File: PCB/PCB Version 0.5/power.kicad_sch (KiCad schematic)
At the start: 31 parts, among them IC5 LMR38025SDRRR, IC6 LMR38025SDRRR, U4 TPS2116DRL, U6 LP5912-3.3DRV, U7 TPS746-3.3DRV

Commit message: wip backup
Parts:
- C72: footprint Capacitor_SMD:C_1210_3225Metric -> Capacitor_SMD:C_0805_2012Metric
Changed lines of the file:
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@@
 			)
 		)
-		(property "Footprint" "Capacitor_SMD:C_1210_3225Metric"
+		(property "Footprint" "Capacitor_SMD:C_0805_2012Metric"
 			(at 147.0152 127 0)
 			(effects

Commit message: wip backup
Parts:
- C67, C70: footprint Capacitor_SMD:C_0402_1005Metric -> Capacitor_SMD:C_0402_1005Metric_Pad0.74x0.62mm_HandSolder
- R15, R16, R19, R20: footprint Resistor_SMD:R_0402_1005Metric -> Resistor_SMD:R_0402_1005Metric_Pad0.72x0.64mm_HandSolder
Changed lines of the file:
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@@
 			)
 		)
-		(property "Footprint" "Resistor_SMD:R_0402_1005Metric"
+		(property "Footprint" "Resistor_SMD:R_0402_1005Metric_Pad0.72x0.64mm_HandSolder"
 			(at 125.222 118.11 90)
 			(effects
@@
 			)
 		)
-		(property "Footprint" "Resistor_SMD:R_0402_1005Metric"
+		(property "Footprint" "Resistor_SMD:R_0402_1005Metric_Pad0.72x0.64mm_HandSolder"
 			(at 125.222 128.27 90)
 			(effects
@@
 			)
 		)
-		(property "Footprint" "Capacitor_SMD:C_0402_1005Metric"
+		(property "Footprint" "Capacitor_SMD:C_0402_1005Metric_Pad0.74x0.62mm_HandSolder"
 			(at 53.0352 68.58 0)
 			(effects
@@
 			)
 		)
-		(property "Footprint" "Capacitor_SMD:C_0402_1005Metric"
+		(property "Footprint" "Capacitor_SMD:C_0402_1005Metric_Pad0.74x0.62mm_HandSolder"
 			(at 53.0352 130.81 0)
 			(effects
@@
 			)
 		)
-		(property "Footprint" "Resistor_SMD:R_0402_1005Metric"
+		(property "Footprint" "Resistor_SMD:R_0402_1005Metric_Pad0.72x0.64mm_HandSolder"
 			(at 125.222 66.04 90)
 			(effects
@@
 			)
 		)
-		(property "Footprint" "Resistor_SMD:R_0402_1005Metric"
+		(property "Footprint" "Resistor_SMD:R_0402_1005Metric_Pad0.72x0.64mm_HandSolder"
 			(at 125.222 55.88 90)
 			(effects

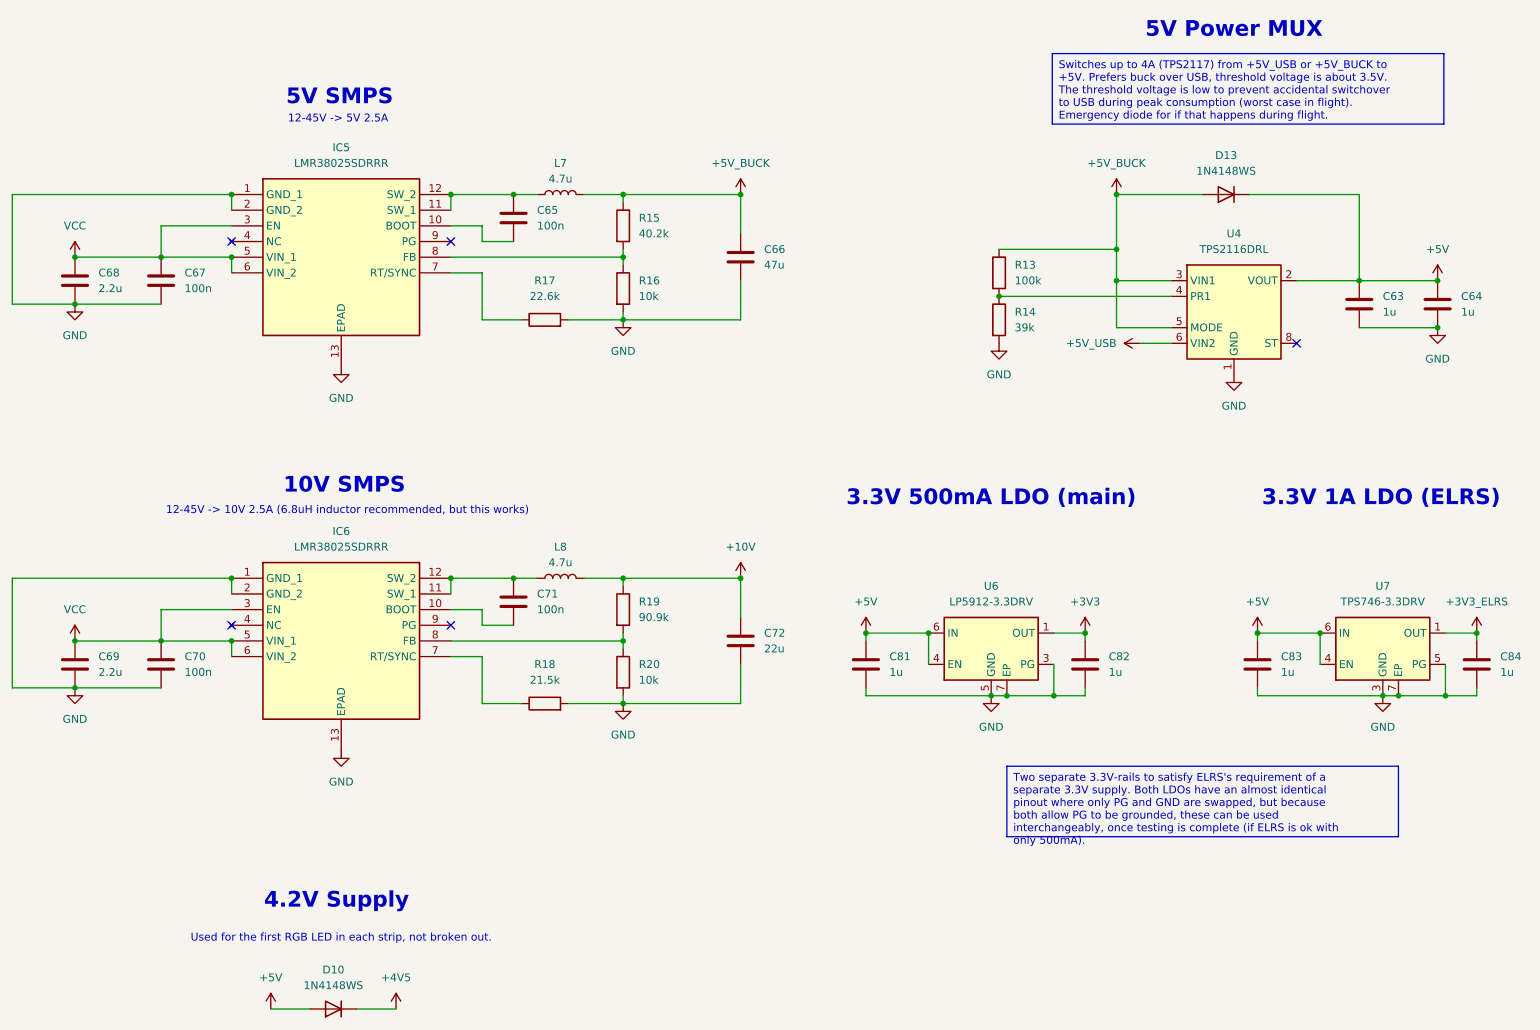
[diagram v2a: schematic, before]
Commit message: preliminary layout
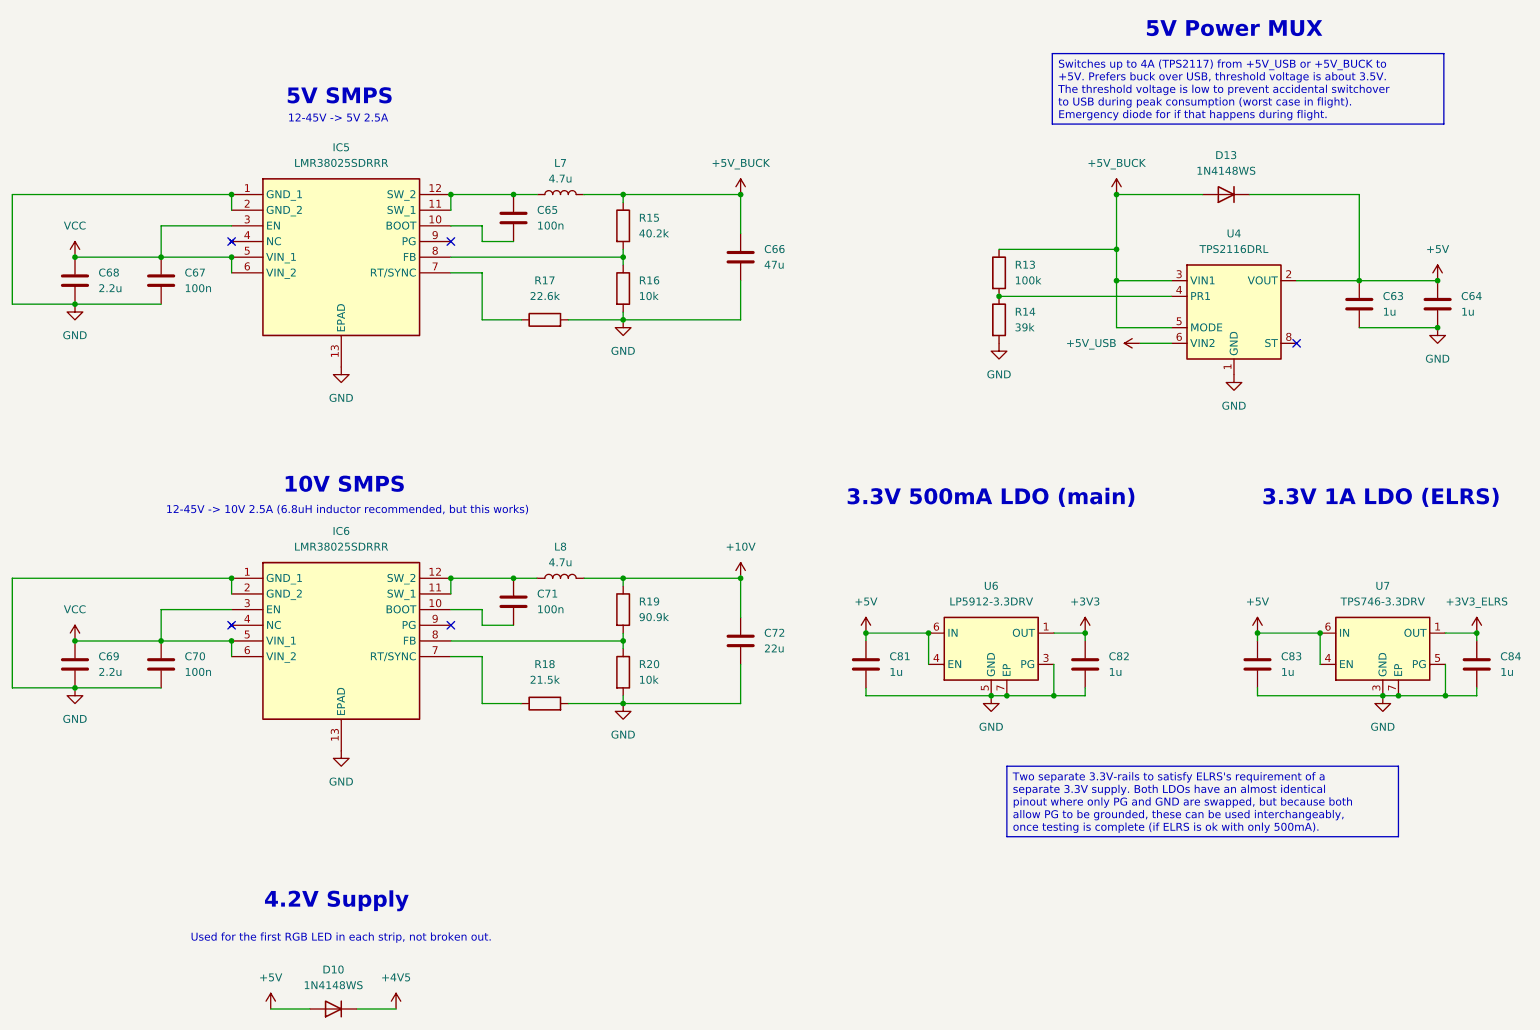
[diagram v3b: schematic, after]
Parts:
- C65, C71, C84: footprint Capacitor_SMD:C_0402_1005Metric -> Capacitor_SMD:C_0402_1005Metric_Pad0.74x0.62mm_HandSolder
- C67: footprint Capacitor_SMD:C_0402_1005Metric_Pad0.74x0.62mm_HandSolder -> Capacitor_SMD:C_0402_1005Metric
- R13, R14, R17, R18: footprint Resistor_SMD:R_0402_1005Metric -> Resistor_SMD:R_0402_1005Metric_Pad0.72x0.64mm_HandSolder
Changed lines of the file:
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@@
 (kicad_sch
-	(version 20231120)
+	(version 20250114)
 	(generator "eeschema")
-	(generator_version "8.0")
+	(generator_version "9.0")
 	(paper "A4")
 	(title_block
 		(title "Kolibri FC - DCDC + LDO")
 	)
+	(text "12-45V -> 10V 2.5A (6.8uH inductor recommended, but this works)"
+		(exclude_from_sim no)
+		(at 82.296 102.108 0)
+		(effects
+			(font
+				(size 1.27 1.27)
+			)
+		)
+	)
+	(text "3.3V 1A LDO (ELRS)"
+		(exclude_from_sim no)
+		(at 249.936 100.076 0)
+		(effects
+			(font
+				(size 2.54 2.54)
+				(thickness 0.508)
+				(bold yes)
+			)
+		)
+	)
+	(text "Used for the first RGB LED in each strip, not broken out."
+		(exclude_from_sim no)
+		(at 81.28 171.45 0)
+		(effects
+			(font
+				(size 1.27 1.27)
+			)
+		)
+	)
+	(text "12-45V -> 5V 2.5A"
+		(exclude_from_sim no)
+		(at 80.772 38.608 0)
+		(effects
+			(font
+				(size 1.27 1.27)
+			)
+		)
+	)
+	(text "3.3V 500mA LDO (main)"
+		(exclude_from_sim no)
+		(at 186.69 100.076 0)
+		(effects
+			(font
+				(size 2.54 2.54)
+				(thickness 0.508)
+				(bold yes)
+			)
+		)
+	)
+	(text "4.2V Supply"
+		(exclude_from_sim no)
+		(at 80.518 165.354 0)
+		(effects
+			(font
+				(size 2.54 2.54)
+				(thickness 0.508)
+				(bold yes)
+			)
+		)
+	)
+	(text "5V SMPS"
+		(exclude_from_sim no)
+		(at 81.026 35.052 0)
+		(effects
+			(font
+				(size 2.54 2.54)
+				(thickness 0.508)
+				(bold yes)
+			)
+		)
+	)
+	(text "5V Power MUX"
+		(exclude_from_sim no)
+		(at 226.06 24.13 0)
+		(effects
+			(font
+				(size 2.54 2.54)
+				(thickness 0.508)
+				(bold yes)
+			)
+		)
+	)
+	(text "10V SMPS"
+		(exclude_from_sim no)
+		(at 81.788 98.044 0)
+		(effects
+			(font
+				(size 2.54 2.54)
+				(thickness 0.508)
+				(bold yes)
+			)
+		)
+	)
+	(text_box "Two separate 3.3V-rails to satisfy ELRS's requirement of a separate 3.3V supply. Both LDOs have an almost identical pinout where only PG and GND are swapped, but because both allow PG to be grounded, these can be used interchangeably, once testing is complete (if ELRS is ok with only 500mA)."
+		(exclude_from_sim no)
+		(at 189.23 143.51 0)
+		(size 63.5 11.43)
+		(margins 0.9525 0.9525 0.9525 0.9525)
+		(stroke
+			(width 0)
+			(type default)
+		)
+		(fill
+			(type none)
+		)
+		(effects
+			(font
+				(size 1.27 1.27)
+			)
+			(justify left top)
+		)
+	)
+	(text_box "Switches up to 4A (TPS2117) from +5V_USB or +5V_BUCK to +5V. Prefers buck over USB, threshold voltage is about 3.5V. The threshold voltage is low to prevent accidental switchover to USB during peak consumption (worst case in flight). Emergency diode for if that happens during flight."
+		(exclude_from_sim no)
+		(at 196.596 27.94 0)
+		(size 63.5 11.43)
+		(margins 0.9525 0.9525 0.9525 0.9525)
+		(stroke
+			(width 0)
+			(type default)
+		)
+		(fill
+			(type none)
+		)
+		(effects
+			(font
+				(size 1.27 1.27)
+			)
+			(justify left top)
+		)
+	)
 	(junction
 		(at 146.05 113.03)
@@
 		)
 	)
-	(text_box "Two separate 3.3V-rails to satisfy ELRS's requirement of a separate 3.3V supply. Both LDOs have an almost identical pinout where only PG and GND are swapped, but because both allow PG to be grounded, these can be used interchangeably, once testing is complete (if ELRS is ok with only 500mA)."
-		(exclude_from_sim no)
-		(at 189.23 143.51 0)
-		(size 63.5 11.43)
-		(stroke
-			(width 0)
-			(type default)
-		)
-		(fill
-			(type none)
-		)
-		(effects
-			(font
-				(size 1.27 1.27)
-			)
-			(justify left top)
-		)
-	)
-	(text_box "Switches up to 4A (TPS2117) from +5V_USB or +5V_BUCK to +5V. Prefers buck over USB, threshold voltage is about 3.5V. The threshold voltage is low to prevent accidental switchover to USB during peak consumption (worst case in flight). Emergency diode for if that happens during flight."
-		(exclude_from_sim no)
-		(at 196.596 27.94 0)
-		(size 63.5 11.43)
-		(stroke
-			(width 0)
-			(type default)
-		)
-		(fill
-			(type none)
-		)
-		(effects
-			(font
-				(size 1.27 1.27)
-			)
-			(justify left top)
-		)
-	)
-	(text "12-45V -> 10V 2.5A (6.8uH inductor recommended, but this works)"
-		(exclude_from_sim no)
-		(at 82.296 102.108 0)
-		(effects
-			(font
-				(size 1.27 1.27)
-			)
-		)
-	)
-	(text "3.3V 1A LDO (ELRS)"
-		(exclude_from_sim no)
-		(at 249.936 100.076 0)
-		(effects
-			(font
-				(size 2.54 2.54)
-				(thickness 0.508)
-				(bold yes)
-			)
-		)
-	)
-	(text "Used for the first RGB LED in each strip, not broken out."
-		(exclude_from_sim no)
-		(at 81.28 171.45 0)
-		(effects
-			(font
-				(size 1.27 1.27)
-			)
-		)
-	)
-	(text "12-45V -> 5V 2.5A"
-		(exclude_from_sim no)
-		(at 80.772 38.608 0)
-		(effects
-			(font
-				(size 1.27 1.27)
-			)
-		)
-	)
-	(text "3.3V 500mA LDO (main)"
-		(exclude_from_sim no)
-		(at 186.69 100.076 0)
-		(effects
-			(font
-				(size 2.54 2.54)
-				(thickness 0.508)
-				(bold yes)
-			)
-		)
-	)
-	(text "4.2V Supply"
-		(exclude_from_sim no)
-		(at 80.518 165.354 0)
-		(effects
-			(font
-				(size 2.54 2.54)
-				(thickness 0.508)
-				(bold yes)
-			)
-		)
-	)
-	(text "5V SMPS"
-		(exclude_from_sim no)
-		(at 81.026 35.052 0)
-		(effects
-			(font
-				(size 2.54 2.54)
-				(thickness 0.508)
-				(bold yes)
-			)
-		)
-	)
-	(text "5V Power MUX"
-		(exclude_from_sim no)
-		(at 226.06 24.13 0)
-		(effects
-			(font
-				(size 2.54 2.54)
-				(thickness 0.508)
-				(bold yes)
-			)
-		)
-	)
-	(text "10V SMPS"
-		(exclude_from_sim no)
-		(at 81.788 98.044 0)
-		(effects
-			(font
-				(size 2.54 2.54)
-				(thickness 0.508)
-				(bold yes)
-			)
-		)
-	)
 	(symbol
 		(lib_id "Device:C")
@@
 			)
 		)
-		(property "Footprint" "Resistor_SMD:R_0402_1005Metric"
+		(property "Footprint" "Resistor_SMD:R_0402_1005Metric_Pad0.72x0.64mm_HandSolder"
 			(at 186.182 63.5 90)
 			(effects
@@
 			)
 		)
-		(property "Footprint" "Resistor_SMD:R_0402_1005Metric"
+		(property "Footprint" "Resistor_SMD:R_0402_1005Metric_Pad0.72x0.64mm_HandSolder"
 			(at 114.3 72.898 90)
 			(effects
@@
 			)
 		)
-		(property "Footprint" "Resistor_SMD:R_0402_1005Metric"
+		(property "Footprint" "Resistor_SMD:R_0402_1005Metric_Pad0.72x0.64mm_HandSolder"
 			(at 114.3 135.128 90)
 			(effects
@@
 			)
 		)
-		(property "Footprint" "Capacitor_SMD:C_0402_1005Metric"
+		(property "Footprint" "Capacitor_SMD:C_0402_1005Metric_Pad0.74x0.62mm_HandSolder"
 			(at 108.2548 113.03 0)
 			(effects
@@
 			)
 		)
-		(property "Footprint" "Capacitor_SMD:C_0402_1005Metric"
+		(property "Footprint" "Capacitor_SMD:C_0402_1005Metric_Pad0.74x0.62mm_HandSolder"
 			(at 266.3952 130.81 0)
 			(effects
@@
 			)
 		)
-		(property "Footprint" "Capacitor_SMD:C_0402_1005Metric_Pad0.74x0.62mm_HandSolder"
+		(property "Footprint" "Capacitor_SMD:C_0402_1005Metric"
 			(at 53.0352 68.58 0)
 			(effects
@@
 			)
 		)
-		(property "Footprint" "Capacitor_SMD:C_0402_1005Metric"
+		(property "Footprint" "Capacitor_SMD:C_0402_1005Metric_Pad0.74x0.62mm_HandSolder"
 			(at 108.2548 50.8 0)
 			(effects
@@
 			)
 		)
-		(property "Footprint" "Resistor_SMD:R_0402_1005Metric"
+		(property "Footprint" "Resistor_SMD:R_0402_1005Metric_Pad0.72x0.64mm_HandSolder"
 			(at 186.182 71.12 90)
 			(effects
